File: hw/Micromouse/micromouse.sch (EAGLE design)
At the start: 4 parts, among them IC1 DSPIC33FJ64MC804-PT, IC2 DRV8833PWR

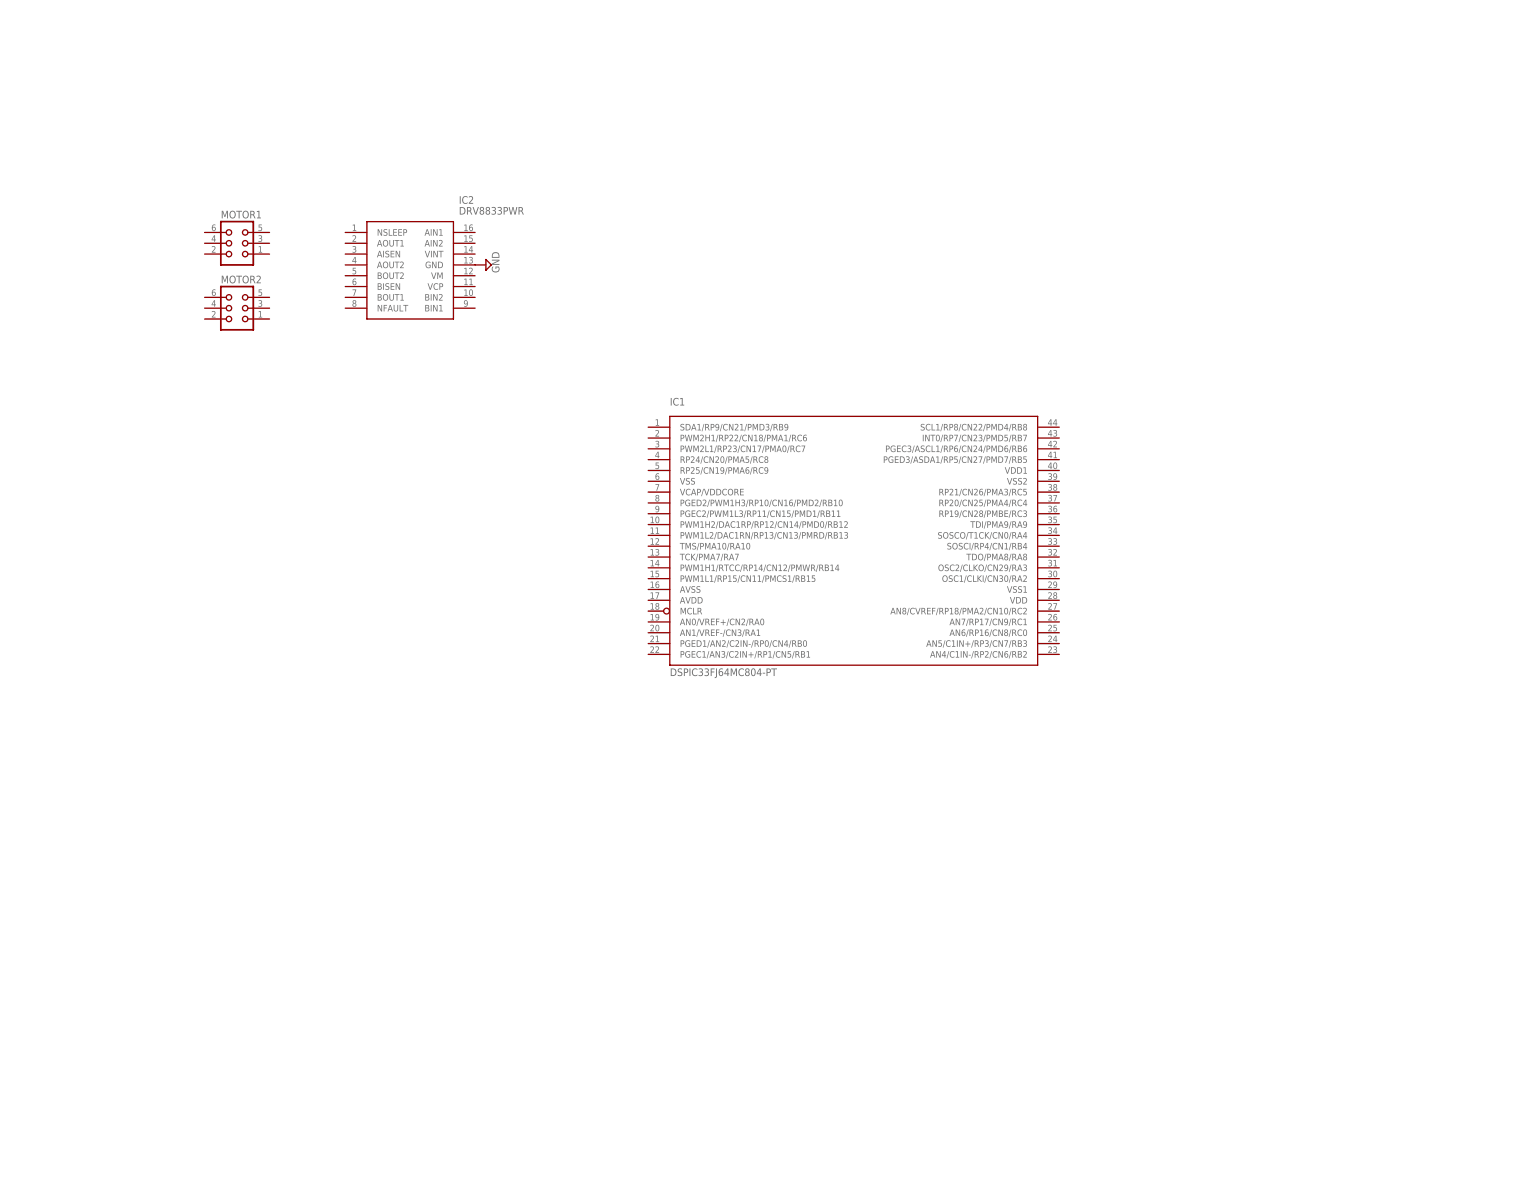
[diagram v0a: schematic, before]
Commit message: Added voltage regulator circuit; Added oscillator configuration; Added parts to library
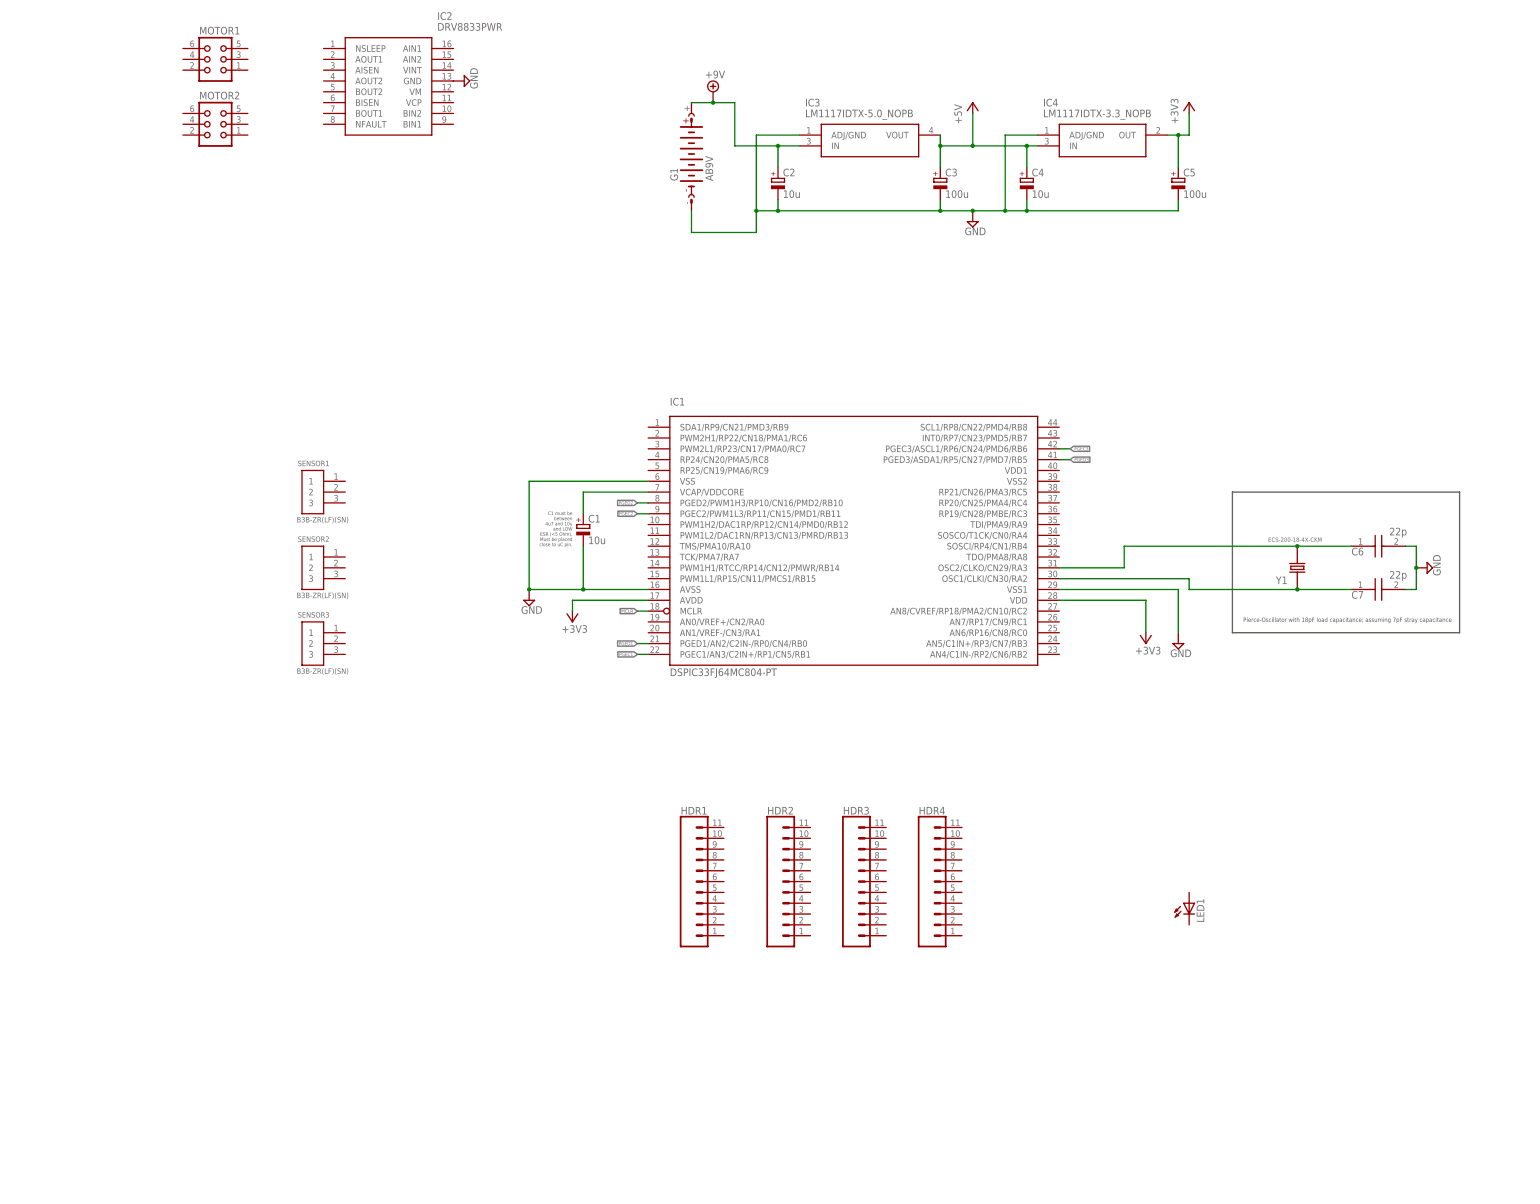
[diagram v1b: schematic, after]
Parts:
- added C1, C2, C4: 10u, micromouse:CPOL_0805
- added C3, C5: 100u, micromouse:CPOL_0805
- added C6, C7: C0805C220F5GACTU, SamacSys_Parts:C0805C220F5GACTU
- added G1: AB9V, battery:AB9V
- added HDR1, HDR2, HDR3, HDR4: (no value), SparkFun-Connectors:CONN_11
- added IC3: LM1117IDTX-5.0_NOPB, SamacSys_Parts:LM1117IDTX-5.0_NOPB
- added IC4: LM1117IDTX-3.3_NOPB, SamacSys_Parts:LM1117IDTX-3.3_NOPB
- added LED1: (no value), adafruit:LED5MM
- added SENSOR1, SENSOR2, SENSOR3: B3B-ZR(LF)(SN), Headers:B3B-ZR(LF)(SN)
- added Y1: ECS-200-18-4X-CKM, ECS-200-18-4X-CKM:ECS-200-18-4X-CKM
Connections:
- new net +3V3: C5.+, IC1.AVDD, IC1.VDD, IC4.OUT
- new net +5V: C3.+, C4.+, IC3.VOUT, IC4.IN
- new net +9V: C2.+, G1.+, IC3.IN
- new net MCLR: IC1.MCLR
- new net N$1: C6.1, IC1.OSC2/CLKO/CN29/RA3, Y1.2
- new net N$2: C7.1, IC1.OSC1/CLKI/CN30/RA2, Y1.1
- new net PGEC1: IC1.PGEC1/AN3/C2IN+/RP1/CN5/RB1
- new net PGEC2: IC1.PGEC2/PWM1L3/RP11/CN15/PMD1/RB11
- new net PGEC3: IC1.PGEC3/ASCL1/RP6/CN24/PMD6/RB6
- new net PGED1: IC1.PGED1/AN2/C2IN-/RP0/CN4/RB0
- new net PGED2: IC1.PGED2/PWM1H3/RP10/CN16/PMD2/RB10
- new net PGED3: IC1.PGED3/ASDA1/RP5/CN27/PMD7/RB5
- new net VCAP/VDDCORE: C1.+, IC1.VCAP/VDDCORE
- net GND: now also C1.-, C2.-, C3.-, C4.-, C5.-, C6.2, C7.2, G1.-, IC1.AVSS, IC1.VSS, IC1.VSS1, IC3.ADJ/GND, IC4.ADJ/GND
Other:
- note added: "C1 must be between 4u7 and 10u and LOW ESR (<5 Ohm). Must be placed close to uC pin."
- note added: "Pierce-Oscillator with 18pF load capacitance; assuming 7pF stray capacitance"
- moved on the sheet: IC2, MOTOR1, MOTOR2

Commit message: Updated schematic
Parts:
- removed HDR3, HDR4: (no value), SparkFun-Connectors:CONN_11
- removed IC3: LM1117IDTX-5.0_NOPB, SamacSys_Parts:LM1117IDTX-5.0_NOPB
- removed IC4: LM1117IDTX-3.3_NOPB, SamacSys_Parts:LM1117IDTX-3.3_NOPB
- removed MOTOR1, MOTOR2: (no value), con-harting:CON06
- removed SENSOR1, SENSOR2, SENSOR3: B3B-ZR(LF)(SN), Headers:B3B-ZR(LF)(SN)
- added C10: 10u, micromouse:CPOL_0805
- added C11, C12: 100n, micromouse:C_0805
- added C8: 0.01u, micromouse:C_0805
- added C9: 2u2, micromouse:C_0805
- added LED2, LED3, LED4, LED5: (no value), micromouse:LED
- added M1, M2: (no value), micromouse:MOTOR_CON
- added R1: 0.2, micromouse:R_0805
- added R10, R2, R4: 10k, micromouse:R_0805
- added R11, R3, R5: 1k, micromouse:R_0805
- added R6, R7, R8, R9: 130, micromouse:R_0805
- added REG1: LM1117-5.0V, micromouse:LM1117_SOT223
- added REG2: LM1117-3.3V, micromouse:LM1117_SOT223
- added S1, S3: GP2Y0A51SK0F, micromouse:SENSOR_CON
- added S2: GP2Y0A41SK0F, micromouse:SENSOR_CON
- added SW1, SW2, SW3: B3F-1000, micromouse:B3F-1000
- added T1, T2, T3, T4: NHDTC1X4ETR, micromouse:NHDTC1X4ETR
- C6, C7: value C0805C220F5GACTU -> 15p; device SamacSys_Parts:C0805C220F5GACTU -> micromouse:C_0805
- HDR1: value (none) -> PICKIT_CON; device SparkFun-Connectors:CONN_11 -> micromouse:PICKIT_CON
- HDR2: value (none) -> UART_CON; device SparkFun-Connectors:CONN_11 -> micromouse:UART_CON
- Y1: value ECS-200-18-4X-CKM -> (none); device ECS-200-18-4X-CKM:ECS-200-18-4X-CKM -> SparkFun-Clocks:CRYSTALPTH-HC49US
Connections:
- removed net N$1: C6.1, IC1.OSC2/CLKO/CN29/RA3, Y1.2
- removed net N$2: C7.1, IC1.OSC1/CLKI/CN30/RA2, Y1.1
- new net LED1: T1.B
- new net LED2: T2.B
- new net LED3: T3.B
- new net LED4: T4.B
- new net M1+: IC2.AOUT1, M1.2
- new net M1-: IC2.AOUT2, M1.1
- new net M1_CHA: M1.5
- new net M1_CHB: M1.6
- new net M1_IN1: IC2.AIN1
- new net M1_IN2: IC2.AIN2
- new net M2+: IC2.BOUT1, M2.2
- new net M2-: IC2.BOUT2, M2.1
- new net M2_CHA: M2.5
- new net M2_CHB: M2.6
- new net M2_IN1: IC2.BIN1
- new net M2_IN2: IC2.BIN2
- new net N$10: R7.2, T2.C
- new net N$11: LED3.C, R7.1
- new net N$12: R8.2, T3.C
- new net N$13: LED4.C, R8.1
- new net N$14: R9.2, T4.C
- new net N$15: LED5.C, R9.1
- new net N$16: C11.+, R10.2, R11.1, SW3.4
- new net N$3: C8.-, IC2.VCP
- new net N$4: C9.+, IC2.VINT
- new net N$5: IC2.AISEN, IC2.BISEN, R1.1
- new net N$6: C12.+, R4.2, R5.1, SW2.4
- new net N$7: R2.2, R3.1, SW1.4
- new net N$8: R6.2, T1.C
- new net N$9: LED2.C, R6.1
- new net OSC1: C7.+, IC1.OSC1/CLKI/CN30/RA2, Y1.1
- new net OSC2: C6.+, IC1.OSC2/CLKO/CN29/RA3, Y1.2
- new net PGC: HDR1.4
- new net PGD: HDR1.5
- new net S1_OUT: S1.1
- new net S2_OUT: S2.3
- new net S3_OUT: S3.1
- new net SW1: R5.2
- new net SW2: R11.2
- new net UART_RX: HDR2.2
- new net UART_TX: HDR2.1
- net +3V3: now also HDR1.2, IC1.VDD1, IC2.NFAULT, IC2.NSLEEP, M1.4, M2.4, R10.1, R2.1, R4.1, REG2.VOUT; no longer IC4.OUT
- net +5V: now also LED2.A, LED3.A, LED4.A, LED5.A, REG1.VOUT, REG2.VIN, S1.3, S2.1, S3.3; no longer IC3.VOUT, IC4.IN
- net +9V: now also C10.+, C8.+, IC2.VM, REG1.VIN; no longer IC3.IN
- net GND: now also C10.-, C11.-, C12.-, C6.-, C7.-, C9.-, HDR1.3, HDR2.3, IC1.VSS2, M1.3, M2.3, R1.2, REG1.GND, REG2.GND, S1.2, S2.2, S3.2, SW1.2, SW2.2, SW3.2, T1.E, T2.E, T3.E, T4.E; no longer C6.2, C7.2, IC3.ADJ/GND, IC4.ADJ/GND
- net MCLR: now also HDR1.1, R3.2
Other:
- note added: "Button design similar to dsPic starter kit"
- note added: "Capacitor is not recommended by the PICKIT Programmer Users Guide"
- note added: "Pierce-Oscillator 16 Mhz"
- note added: "Resistor limits motor supply current to 1A. <Resistor value> = 0.2V / I_chop"
- note added: "S1 = Left (2-15cm) S2 = Mid (4-30cm) S3 = Right (2-15cm)"
- note added: "put bypass on motors?"
- note removed: "Pierce-Oscillator with 18pF load capacitance; assuming 7pF stray capacitance"
- moved on the sheet: G1, IC1, IC2, LED1

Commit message: Updated EAGLE project
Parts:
- removed S1, S3: GP2Y0A51SK0F, micromouse:SENSOR_CON
- removed S2: GP2Y0A41SK0F, micromouse:SENSOR_CON
- added J1, J2: GP2Y0A51SK0F, micromouse:B3B-ZR
- added J3: GP2Y0A41SK0F, micromouse:B3B-PH-K-S
- added R12: 0.2, micromouse:R_0805
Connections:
- new net N$1: IC2.BISEN, R12.1
- net +5V: now also J1.1, J2.1, J3.3; no longer S1.3, S2.1, S3.3
- net GND: now also J1.2, J2.2, J3.2, R12.2; no longer S1.2, S2.2, S3.2
- net N$5: no longer IC2.BISEN
- net S1_OUT: now also J1.3; no longer S1.1
- net S2_OUT: now also J3.1; no longer S2.3
- net S3_OUT: now also J2.3; no longer S3.1
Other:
- note added: "S1 = Right (2-15cm) S2 = Mid (4-30cm) S3 = Left (2-15cm)"
- note removed: "S1 = Left (2-15cm) S2 = Mid (4-30cm) S3 = Right (2-15cm)"

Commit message: First routing on PCB
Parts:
- removed R10: 10k, micromouse:R_0805
- removed R11: 1k, micromouse:R_0805
- removed SW2, SW3: B3F-1000, micromouse:B3F-1000
- added C13, C14: (no value), micromouse:C_0805
- added SW_RST: B3F-1000, micromouse:B3F-1000
- C11: value 100n -> (none)
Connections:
- removed net N$16: C11.+, R10.2, R11.1, SW3.4
- removed net PGC: HDR1.4
- removed net PGD: HDR1.5
- removed net PGEC1: IC1.PGEC1/AN3/C2IN+/RP1/CN5/RB1
- removed net PGED1: IC1.PGED1/AN2/C2IN-/RP0/CN4/RB0
- removed net SW2: R11.2
- net +3V3: now also C11.+, C13.-, C14.-; no longer R10.1
- net GND: now also C13.+, C14.+, SW_RST.2; no longer SW2.2, SW3.2
- net M1_CHA: now also IC1.RP19/CN28/PMBE/RC3, M1.6; no longer M1.5
- net M1_CHB: now also IC1.RP20/CN25/PMA4/RC4, M1.5; no longer M1.6
- net M1_IN1: now also IC1.SDA1/RP9/CN21/PMD3/RB9
- net M1_IN2: now also IC1.PWM2H1/RP22/CN18/PMA1/RC6
- net M2_CHA: now also IC1.INT0/RP7/CN23/PMD5/RB7, M2.6; no longer M2.5
- net M2_CHB: now also IC1.SCL1/RP8/CN22/PMD4/RB8, M2.5; no longer M2.6
- net M2_IN1: now also IC1.RP24/CN20/PMA5/RC8
- net M2_IN2: now also IC1.PWM2L1/RP23/CN17/PMA0/RC7
- net N$6: now also SW1.4; no longer SW2.4
- net N$7: now also SW_RST.4; no longer SW1.4
- net PGEC3: now also HDR1.5
- net PGED3: now also HDR1.4
- net S1_OUT: now also IC1.AN1/VREF-/CN3/RA1
- net S2_OUT: now also IC1.PGED1/AN2/C2IN-/RP0/CN4/RB0
- net S3_OUT: now also IC1.PGEC1/AN3/C2IN+/RP1/CN5/RB1
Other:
- note added: "Set VCFG to use AVSS and AVDD VCFG = 0x000"
- note added: "replace with Bluetooth con"
- moved on the sheet: C1, C11, HDR1, HDR2, IC1, LED1, LED2, LED3, LED4, LED5, R6, R7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

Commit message: Added Bluetooth module
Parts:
- HDR2: value UART_CON -> BLUETOOTH; device micromouse:UART_CON -> micromouse:BLUETOOTHSHIELD
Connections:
- removed net PGEC2: IC1.PGEC2/PWM1L3/RP11/CN15/PMD1/RB11
- removed net PGED2: IC1.PGED2/PWM1H3/RP10/CN16/PMD2/RB10
- new net BT_CTS: HDR2.2, IC1.PGED2/PWM1H3/RP10/CN16/PMD2/RB10
- new net BT_MOD: HDR2.1
- new net BT_RTS: HDR2.6, IC1.PWM1L2/DAC1RN/RP13/CN13/PMRD/RB13
- net +3V3: now also HDR2.5, HDR2.8
- net GND: now also HDR2.7; no longer HDR2.3
- net UART_RX: now also HDR2.3, IC1.PGEC2/PWM1L3/RP11/CN15/PMD1/RB11; no longer HDR2.2
- net UART_TX: now also HDR2.4, IC1.PWM1H2/DAC1RP/RP12/CN14/PMD0/RB12; no longer HDR2.1
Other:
- note added: "DFU pin (8) of BT module set high"
- note added: "TX and RX of BT module become RX and TX for the controller"
- note removed: "replace with Bluetooth con"
- moved on the sheet: C14

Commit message: Tighter layout for PCB; Removed transistors for LEDs
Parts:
- removed LED2, LED3, LED4, LED5: (no value), micromouse:LED
- removed T1, T2, T3, T4: NHDTC1X4ETR, micromouse:NHDTC1X4ETR
- added D1, D2, D3, D4: LED_0805, micromouse:LED_0805
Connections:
- removed net N$10: R7.2, T2.C
- removed net N$11: LED3.C, R7.1
- removed net N$12: R8.2, T3.C
- removed net N$14: R9.2, T4.C
- removed net N$8: R6.2, T1.C
- new net N$2: D2.C, R7.1
- net +3V3: now also D1.A, D2.A, D3.A, D4.A
- net +5V: no longer LED2.A, LED3.A, LED4.A, LED5.A
- net BT_CTS: now also IC1.RP21/CN26/PMA3/RC5; no longer IC1.PGED2/PWM1H3/RP10/CN16/PMD2/RB10
- net BT_RTS: now also IC1.SCL1/RP8/CN22/PMD4/RB8; no longer IC1.PWM1L2/DAC1RN/RP13/CN13/PMRD/RB13
- net GND: no longer T1.E, T2.E, T3.E, T4.E
- net LED1: now also IC1.AN4/C1IN-/RP2/CN6/RB2, R6.2; no longer T1.B
- net LED2: now also IC1.AN5/C1IN+/RP3/CN7/RB3, R7.2; no longer T2.B
- net LED3: now also IC1.AN6/RP16/CN8/RC0, R8.2; no longer T3.B
- net LED4: now also IC1.AN7/RP17/CN9/RC1, R9.2; no longer T4.B
- net M1_CHA: now also IC1.PWM1H2/DAC1RP/RP12/CN14/PMD0/RB12; no longer IC1.RP19/CN28/PMBE/RC3
- net M1_CHB: now also IC1.PWM1L2/DAC1RN/RP13/CN13/PMRD/RB13; no longer IC1.RP20/CN25/PMA4/RC4
- net M1_IN1: now also IC1.PWM2L1/RP23/CN17/PMA0/RC7; no longer IC1.SDA1/RP9/CN21/PMD3/RB9
- net M1_IN2: now also IC1.RP24/CN20/PMA5/RC8; no longer IC1.PWM2H1/RP22/CN18/PMA1/RC6
- net M2_CHA: now also IC1.SDA1/RP9/CN21/PMD3/RB9; no longer IC1.INT0/RP7/CN23/PMD5/RB7
- net M2_CHB: now also IC1.PWM2H1/RP22/CN18/PMA1/RC6; no longer IC1.SCL1/RP8/CN22/PMD4/RB8
- net M2_IN1: now also IC1.PGEC2/PWM1L3/RP11/CN15/PMD1/RB11; no longer IC1.RP24/CN20/PMA5/RC8
- net M2_IN2: now also IC1.PGED2/PWM1H3/RP10/CN16/PMD2/RB10; no longer IC1.PWM2L1/RP23/CN17/PMA0/RC7
- net N$13: now also D3.C; no longer LED4.C
- net N$15: now also D4.C; no longer LED5.C
- net N$9: now also D1.C; no longer LED2.C
- net SW1: now also IC1.RP19/CN28/PMBE/RC3
- net UART_RX: now also IC1.RP20/CN25/PMA4/RC4; no longer IC1.PGEC2/PWM1L3/RP11/CN15/PMD1/RB11
- net UART_TX: now also IC1.INT0/RP7/CN23/PMD5/RB7; no longer IC1.PWM1H2/DAC1RP/RP12/CN14/PMD0/RB12
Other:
- moved on the sheet: C13, R6, R7, R8, R9
